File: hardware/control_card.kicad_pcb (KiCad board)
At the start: 6 copper layers, 32.5 x 33.8 mm, 149 parts, among them J1 Power board, J2 JTAG, U1 A3CZ065BB18AE7S, U10 SN74LV4051APWR, U11 OPA365AIDBVR, U12 ADS7056IRUGR, U13 SN74LV4051APWR, U14 OPA365AIDBVR, U15 ADS7056IRUGR, U16 TLV75518PDBVR, U2 AP61302Z6-7, U3 AP61102Z6-7, U4 AP61102Z6-7, U5 TLV75512PDBVR, U6 TLV75533PDBVR, U7 MT25QU256ABA8E12-1SIT, U8 SN74AVC4T774RSVR, U9 W958D8NBYA5I, X1 100MHz

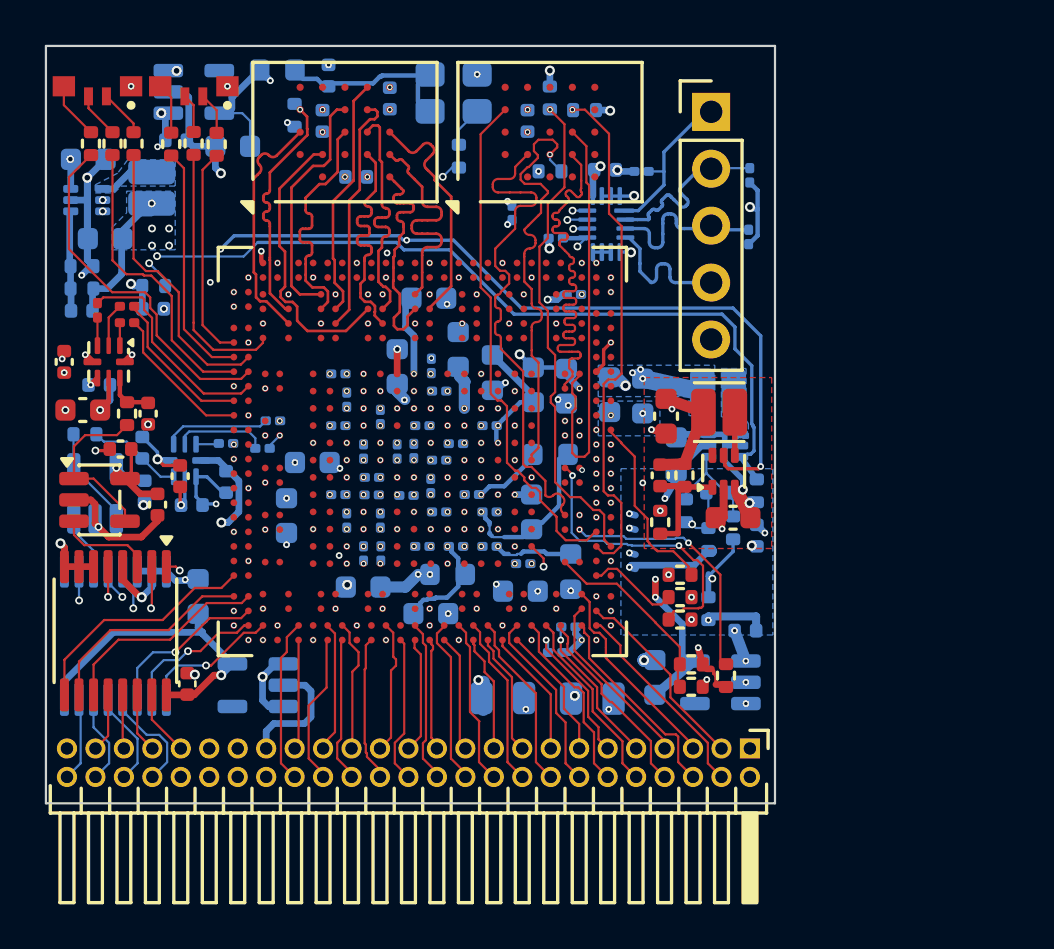
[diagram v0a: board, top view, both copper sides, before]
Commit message: remove ldos and replace with switchers
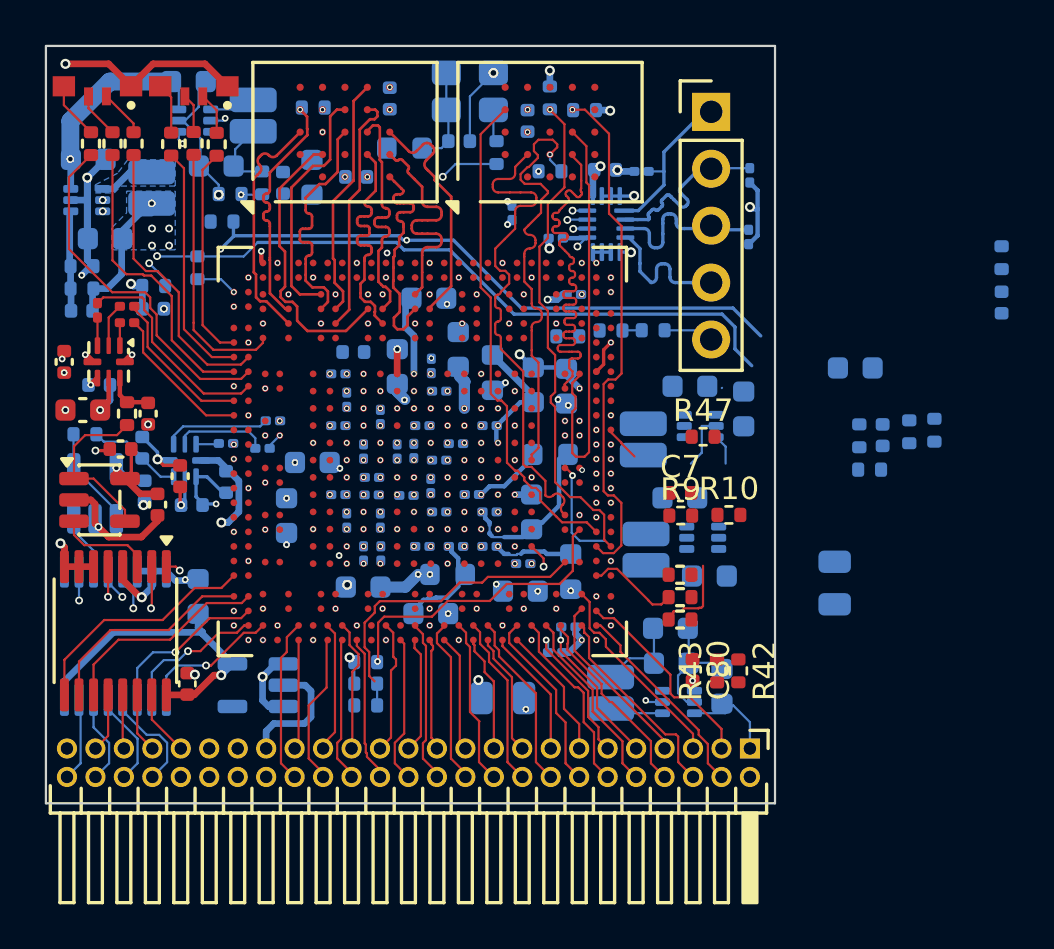
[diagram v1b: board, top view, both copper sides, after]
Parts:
- removed C10, C74: 1u, Capacitor_SMD:C_0402_1005Metric
- removed U16: TLV75518PDBVR, Package_TO_SOT_SMD:SOT-23-5
- removed U5: TLV75512PDBVR, Package_TO_SOT_SMD:SOT-23-5
- added C80: 33p, Capacitor_SMD:C_0402_1005Metric, F.Cu at (104.1, 122.8)
- added C81: 10u, Capacitor_SMD:C_0603_1608Metric, B.Cu at (105.4, 123.5)
- added C82: 22u, Capacitor_SMD:C_0603_1608Metric, B.Cu at (103.1, 120.9)
- added C83: 33p, Capacitor_SMD:C_0402_1005Metric, B.Cu at (85.8, 101.0)
- added C84: 10u, Capacitor_SMD:C_0603_1608Metric, B.Cu at (81.6, 96.5)
- added C85: 22u, Capacitor_SMD:C_0603_1608Metric, B.Cu at (82.8, 100.3)
- added L4: 1u, Inductor_SMD:L_Cenker_CKCS201610, B.Cu at (100.4, 123.8)
- added L5: 1u, Inductor_SMD:L_Cenker_CKCS201610, B.Cu at (84.5, 98.0)
- added R42: 200k, Resistor_SMD:R_0402_1005Metric, F.Cu at (106.1, 122.8)
- added R43: 200k, Resistor_SMD:R_0402_1005Metric, F.Cu at (105.2, 122.8)
- added R44: 200k, Resistor_SMD:R_0402_1005Metric, B.Cu at (84.8, 101.0)
- added R45: 100k, Resistor_SMD:R_0402_1005Metric, B.Cu at (83.4, 101.5)
- added R46: 100k, Resistor_SMD:R_0402_1005Metric, B.Cu at (98.5, 107.9)
- added R47: 200k, Resistor_SMD:R_0402_1005Metric, F.Cu at (104.5, 112.3)
- added R48: 200k, Resistor_SMD:R_0402_1005Metric, B.Cu at (82.0, 104.8)
- added R49: 200k, Resistor_SMD:R_0402_1005Metric, B.Cu at (83.1, 102.7)
- added R50: 100k, Resistor_SMD:R_0402_1005Metric, B.Cu at (100.4, 107.6)
- added R51: 200k, Resistor_SMD:R_0402_1005Metric, B.Cu at (102.3, 107.6)
- added U17: AP61102Z6-7, Package_TO_SOT_SMD:SOT-563, B.Cu at (103.4, 124.2)
- added U18: AP61102Z6-7, Package_TO_SOT_SMD:SOT-563, B.Cu at (81.8, 98.2)
- C8, C9, L3, R12, R13, R14, U4: moved to B.Cu
- moved R12 16.1 mm to (89.5, 122.4), turned to 0 degrees
- moved C16 15.1 mm to (117.8, 106.3)
- moved R5 15.1 mm to (117.8, 104.3)
- moved R14 14.6 mm to (89.5, 123.4), turned to 0 degrees
- moved R13 14.6 mm to (89.5, 124.3), turned to 180 degrees
- moved R4 12.9 mm to (114.8, 112.0), turned to 90 degrees
- moved C14 12.0 mm to (110.4, 118.9), turned to 90 degrees
- moved C52 10.4 mm to (88.9, 108.6), turned to 180 degrees
- moved C2 9.57 mm to (111.3, 109.3), turned to 0 degrees
- moved R2 8.96 mm to (113.7, 112.1)
- moved R1 8.43 mm to (111.5, 112.3)
- moved R3 7.84 mm to (112.0, 113.8), turned to 180 degrees
- moved C77 7.82 mm to (112.5, 112.3), turned to 90 degrees
- moved L3 6.95 mm to (102.0, 117.4), turned to 90 degrees
- moved FB5 6.66 mm to (91.2, 99.5)
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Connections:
- U1 pad BN16: unconnected-(U1H_6F-6F_IO_HVIO_6F_1_TXCLK1_Data_Ctrl1-PadBN16) -> J1_P28
- U1 pad BN19: J1_P28 -> unconnected-(U1C_6A-6A_IO_HVIO_6A_19_TXCLK19_Data_Ctrl19-PadBN19)
- U2 pad 5: +5V -> /Power/EN_0V75
- U4 pad 6: unconnected-(U4-PG-Pad6) -> /Power/PG_3V3
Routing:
- net +0V75: track 14.8 -> 5.35 mm, vias 37 -> 31
- net /Power/PG_1V8: track 47.9 -> 40.8 mm, vias 6 -> 5
- net /Configuration/RREF_SDM: track 7.97 -> 1.52 mm
- net /Power/FB_3V3: track 6.05 -> 0.00 mm
- net /Configuration/MSEL2: track 7.98 -> 14.0 mm
- net GND: track 70.3 -> 76.3 mm, vias 181 -> 164
- net +5V: track 76.0 -> 81.7 mm, vias 8 -> 4
- net /Power/PG_0V75: track 39.6 -> 34.1 mm
- net /Power/FB_1V8HR: track 0.00 -> 5.10 mm, vias 0 -> 2
- net /Configuration/NSTATUS: track 12.8 -> 7.90 mm, vias 2 -> 1
- net /Power/FB_0V75: track 4.75 -> 0.00 mm
- net VCC_SENSE_N: track 17.5 -> 14.1 mm, vias 2 -> 1
- net /Configuration/MSEL1: track 10.9 -> 13.4 mm, vias 2 -> 1
- net +1V2: track 10.7 -> 8.27 mm, vias 8 -> 6
- net /Power/PG_3V3: track 0.00 -> 2.33 mm, vias 0 -> 2
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- removed copper zone on B.Cu, net +0V75
- removed copper zone on B.Cu, net /Power/SW_0V75
- removed copper zone on B.Cu, net GND
- removed copper zone on F.Cu, net GND

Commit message: finish placing components
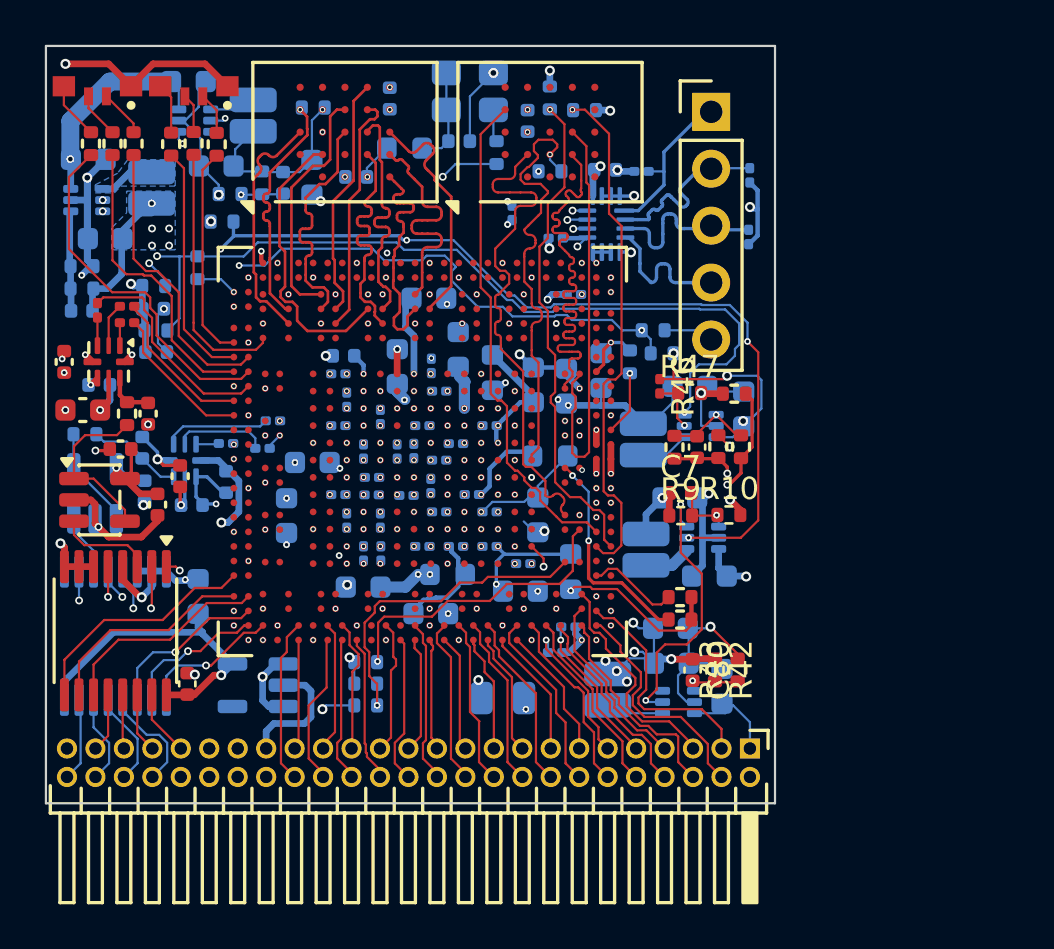
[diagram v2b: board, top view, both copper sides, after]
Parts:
- removed C14: 22u, Capacitor_SMD:C_0805_2012Metric
- C77, R1, R2, R3, R4: moved to F.Cu
- R19: moved to B.Cu
- R46: footprint Resistor_SMD:R_0402_1005Metric -> Resistor_SMD:R_0201_0603Metric; moved to F.Cu
- moved R5 37.9 mm to (80.1, 107.6), turned to 0 degrees
- moved C16 37.8 mm to (80.1, 108.6), turned to 0 degrees
- moved C2 11.4 mm to (100.0, 109.4), turned to 90 degrees
- moved R19 9.76 mm to (101.3, 109.0), turned to 90 degrees
- moved R4 9.08 mm to (105.9, 110.4), turned to 180 degrees
- moved C77 8.30 mm to (104.3, 112.8)
- moved R1 8.27 mm to (103.2, 112.8)
- moved R2 7.54 mm to (106.2, 112.8)
- moved R3 6.83 mm to (105.2, 112.8), turned to -90 degrees
- moved R46 4.67 mm to (102.6, 110.1), turned to -90 degrees
- moved R50 2.50 mm to (102.7, 108.6), turned to 180 degrees
- moved R47 2.04 mm to (103.9, 110.4)
- moved R42 1.04 mm to (105.1, 122.8)
- moved R43 0.92 mm to (106.1, 122.8)
- moved C52 0.47 mm to (88.5, 108.7)
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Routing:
- net /Power/PG_3V3: track 2.33 -> 50.7 mm, vias 2 -> 5
- net GND: track 76.3 -> 97.1 mm, vias 164 -> 169
- net +5V: track 81.7 -> 100.7 mm, vias 4 -> 8
- net +0V75: track 5.35 -> 17.6 mm, vias 31 -> 32
- net /Power/PG_1V8: track 40.8 -> 52.7 mm, vias 5 -> 7
- net +1V8: track 14.6 -> 23.0 mm
- net +1V8_HR: track 3.20 -> 10.9 mm
- net /Power/PG_0V75: track 34.1 -> 41.7 mm, vias 2 -> 3
- net +1V2: track 8.27 -> 15.2 mm, vias 6 -> 12
- net /Power/FB_0V75: track 0.00 -> 3.82 mm, vias 0 -> 1
- net VCC_SENSE_N: track 14.1 -> 17.6 mm, vias 1 -> 2
- net +3V3: track 19.7 -> 23.1 mm, vias 21 -> 22
- net VCC_SENSE_P: track 12.8 -> 15.9 mm, vias 1 -> 2
- net /Power/FB_3V3: track 0.00 -> 2.72 mm, vias 0 -> 1
- net /Power/EN_0V75: track 0.00 -> 2.48 mm, vias 0 -> 1
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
